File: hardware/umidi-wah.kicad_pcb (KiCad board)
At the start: 2 copper layers, 100.7 x 113.4 mm, 83 parts, among them J1 Conn_01x02, J11 Pots Main, J12 Pots Front, J4 Conn_01x02, J5 Input, J6 Output, J7 Conn_02x05_Odd_Even, J8 Conn_02x05_Odd_Even, K1 G6K-2P-Y-DC5, Q1 KSC1815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

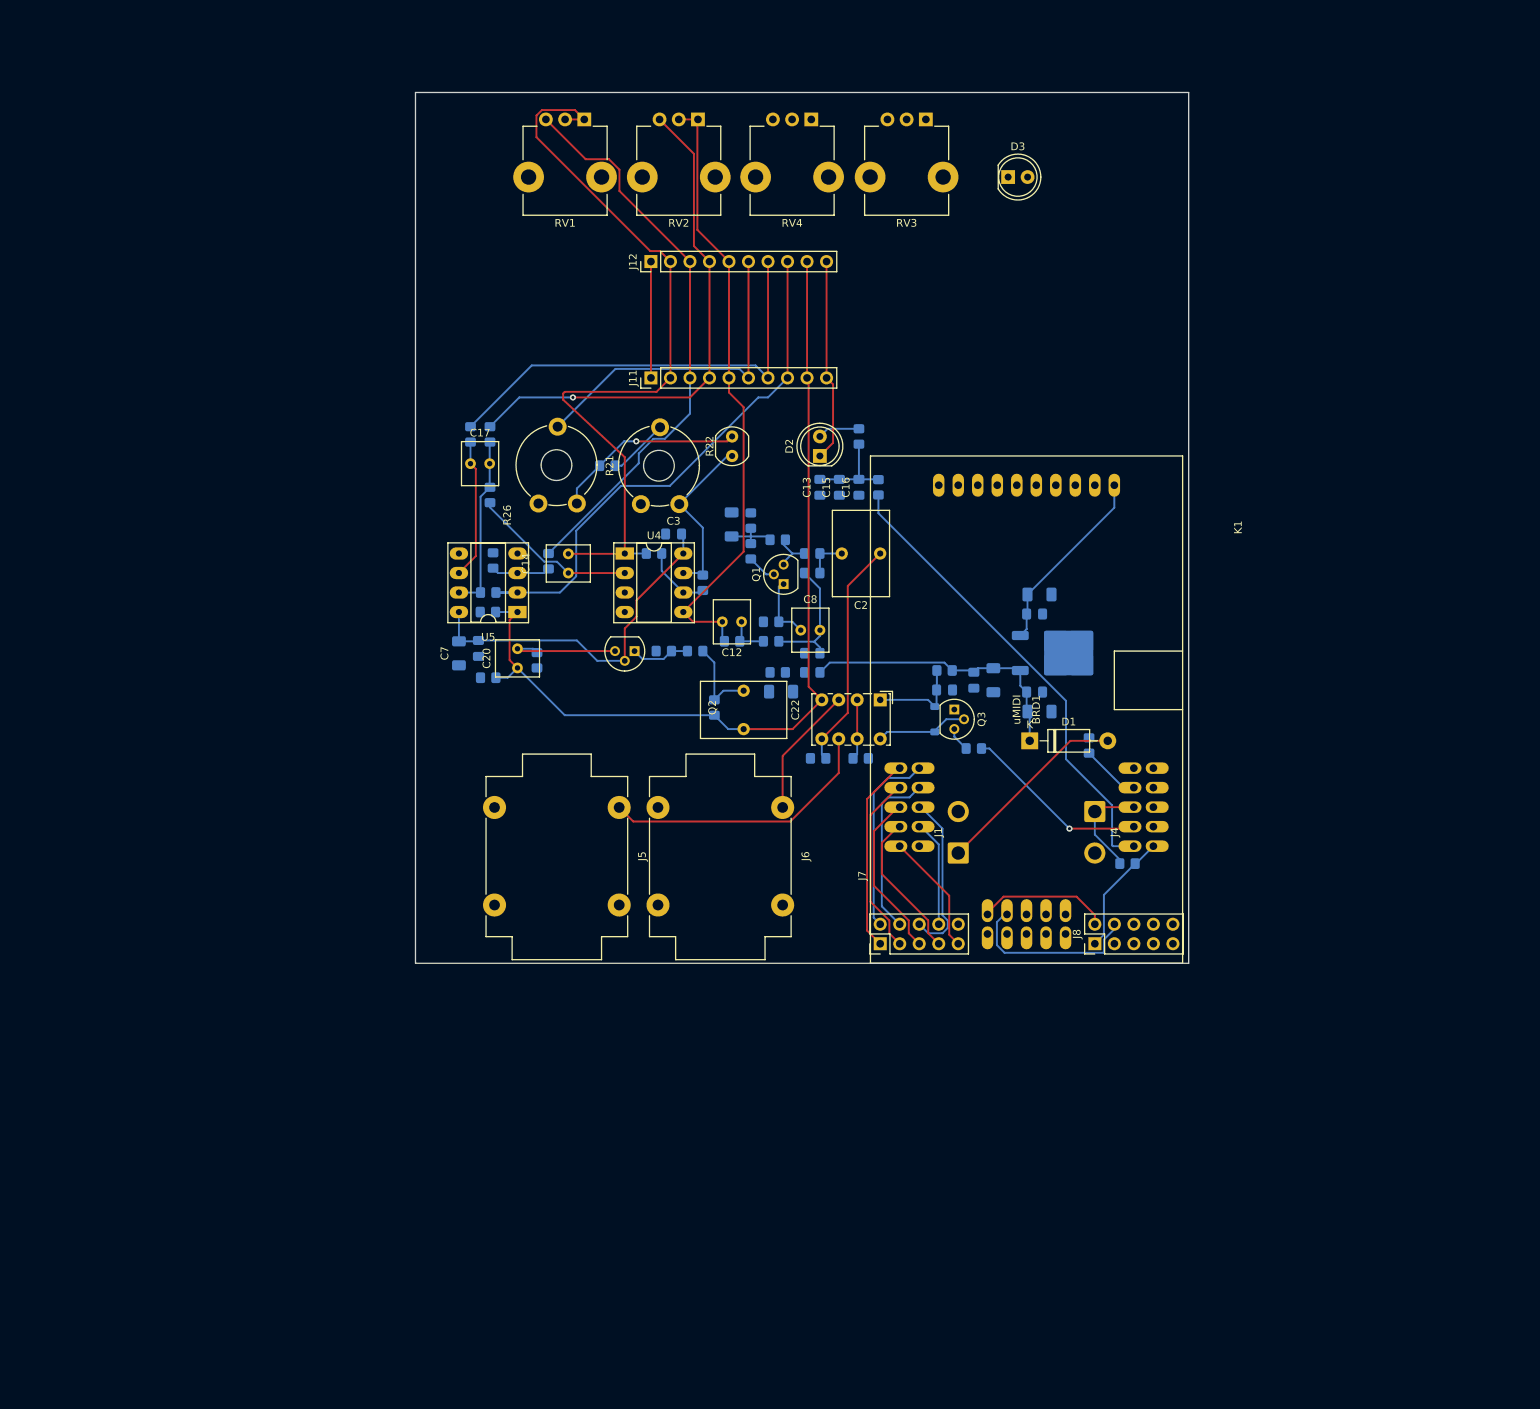
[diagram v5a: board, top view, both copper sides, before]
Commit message: Route pretty much everything
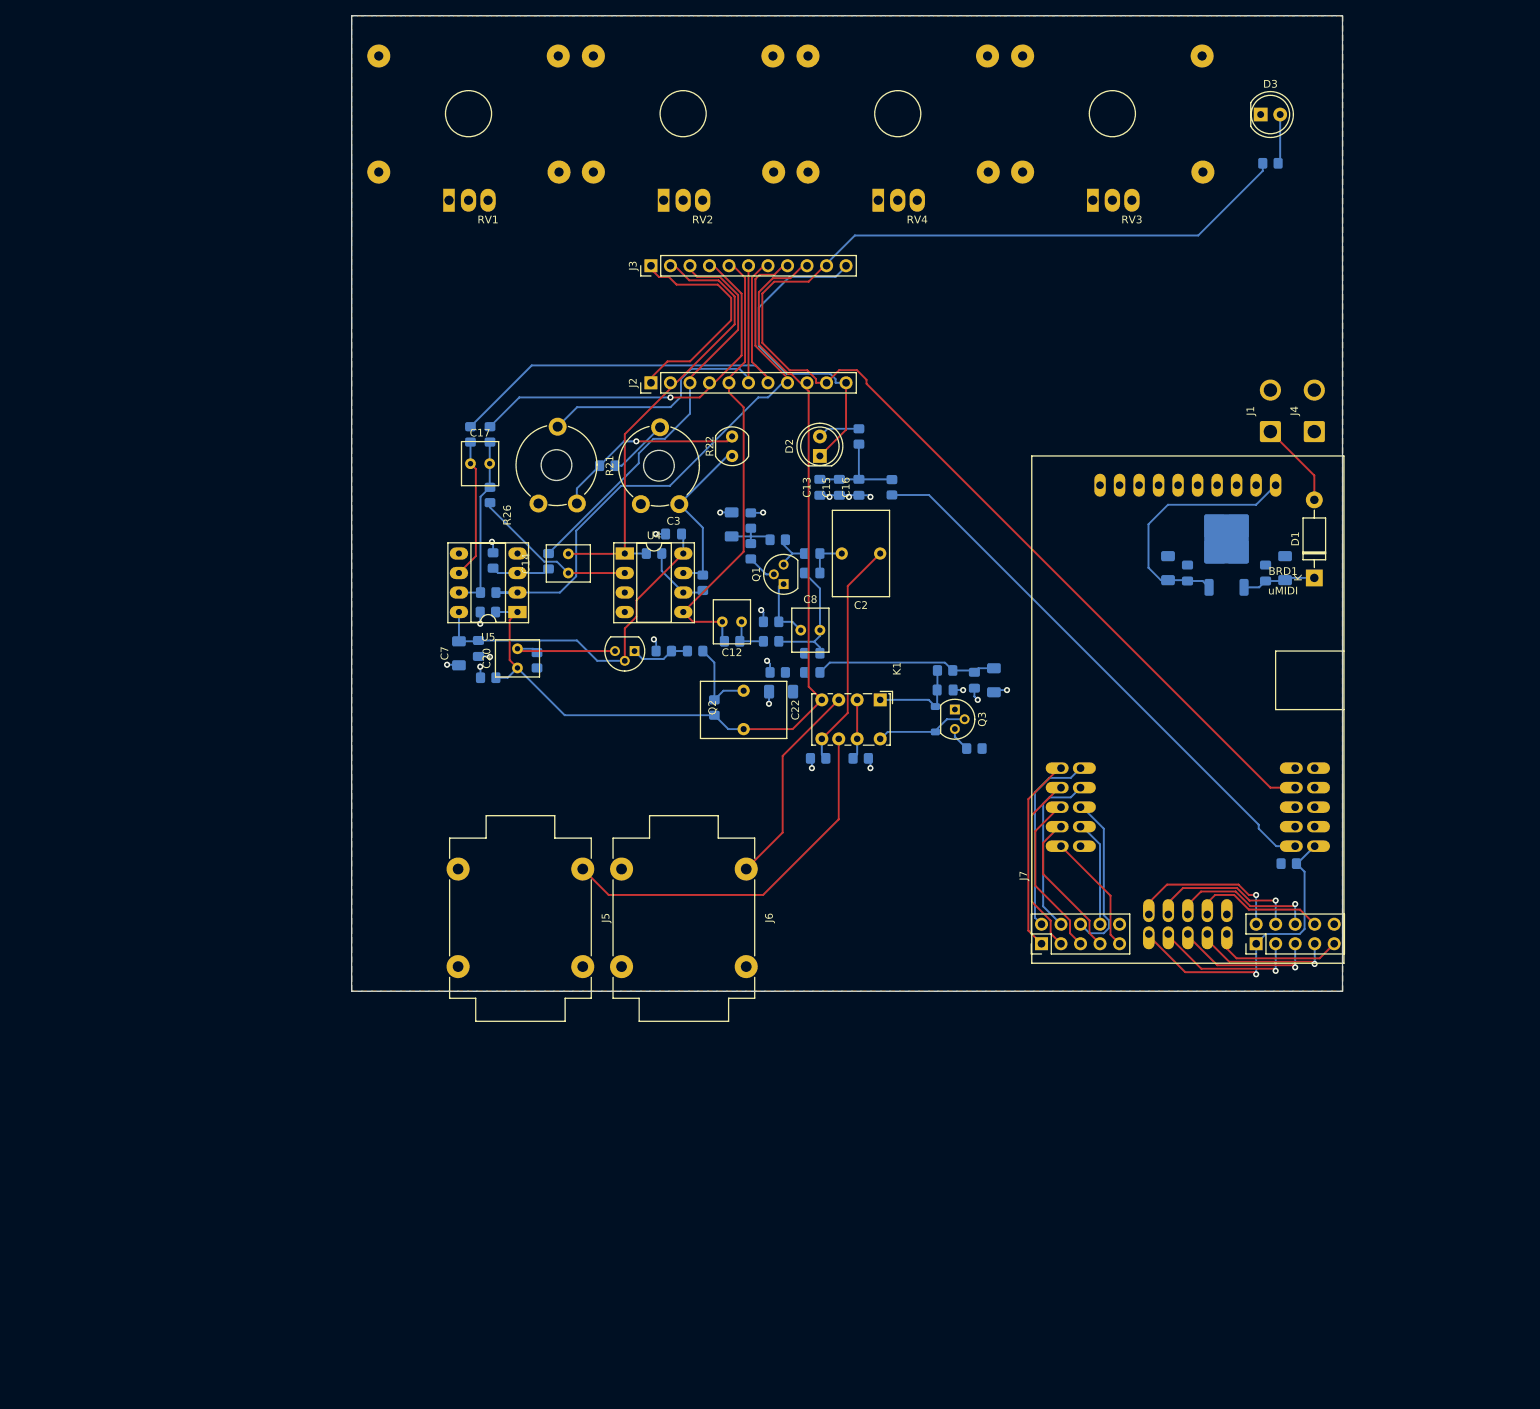
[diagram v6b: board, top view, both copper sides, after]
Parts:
- removed J11: Pots Main, Connector_PinHeader_2.54mm:PinHeader_1x10_P2.54mm_Vertical
- removed J12: Pots Front, Connector_PinHeader_2.54mm:PinHeader_1x10_P2.54mm_Vertical
- added J2: Pots Main, Connector_PinHeader_2.54mm:PinHeader_1x11_P2.54mm_Vertical, F.Cu at (101.0, 57.8)
- added J3: Pots Front, Connector_PinHeader_2.54mm:PinHeader_1x11_P2.54mm_Vertical, F.Cu at (101.0, 42.5)
- J1: value Conn_01x02 -> Power
- J4: value Conn_01x02 -> Switch
- RV1, RV2, RV3, RV4: footprint Potentiometer_THT:Potentiometer_TT_P0915N -> uMidi-wah:Bourns PC Axial Rear Mounting Bracket
- moved R24 79.4 mm to (181.6, 29.2), turned to 180 degrees
- moved J1 68.3 mm to (181.6, 64.1)
- moved J4 57.1 mm to (187.3, 64.1), turned to 90 degrees
- moved D1 42.7 mm to (187.3, 83.2), turned to 90 degrees
- moved C4 37.0 mm to (183.5, 81.9), turned to 90 degrees
- moved D3 33.9 mm to (180.3, 22.9)
- moved C5 33.8 mm to (181.0, 82.5), turned to 90 degrees
- moved RV3 26.5 mm to (161.0, 34.0), turned to 0 degrees
- moved U3 25.7 mm to (175.9, 79.4), turned to 90 degrees
- moved BRD1 21.0 mm to (170.9, 100.3)
- moved J7 21.0 mm to (151.8, 130.8)
- moved J8 21.0 mm to (179.8, 130.8)
- moved R25 21.0 mm to (184.0, 120.4)
- moved C9 20.6 mm to (170.8, 82.5), turned to 90 degrees
- moved RV1 18.4 mm to (77.2, 34.0), turned to 0 degrees
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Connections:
- net /status_led renamed /Filter/status_led
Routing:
- net /Filter/status_led: track 7.69 -> 175.8 mm
- net GND: track 41.5 -> 105.8 mm, vias 0 -> 20
- net /Filter/rv1_1: track 101.0 -> 59.8 mm
- net /bypass_n: track 24.9 -> 0.60 mm, vias 1 -> 0
- net /umidi_3v3: track 41.4 -> 65.1 mm, vias 0 -> 1
- net /Filter/rv1_2: track 75.0 -> 52.8 mm
- net /Filter/rv2_1: track 80.7 -> 59.7 mm
- net Net-(BRD1C-PB1): track 0.00 -> 19.6 mm, vias 0 -> 1
- net Net-(BRD1C-PC0(SDA)): track 0.00 -> 19.5 mm, vias 0 -> 1
- net Net-(BRD1C-PB3(DACB::DAC1)): track 0.00 -> 19.0 mm, vias 0 -> 1
- net Net-(BRD1C-PC1(SCL)): track 0.00 -> 18.7 mm, vias 0 -> 1
- net Net-(BRD1C-PC2(C0::RXD0)): track 0.00 -> 17.5 mm
- net Net-(BRD1C-PC3(C0::TXD0)): track 0.00 -> 17.2 mm
- net /Filter/rv2_2: track 67.5 -> 50.6 mm
- net Net-(D1-A): track 25.5 -> 11.3 mm
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- added copper zone on B.Cu, net GND
- added copper zone on F.Cu, net GND
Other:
- board size 100.7 x 113.4 mm -> 129 x 127 mm

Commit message: Replace bourns potentiometers in schematic and board
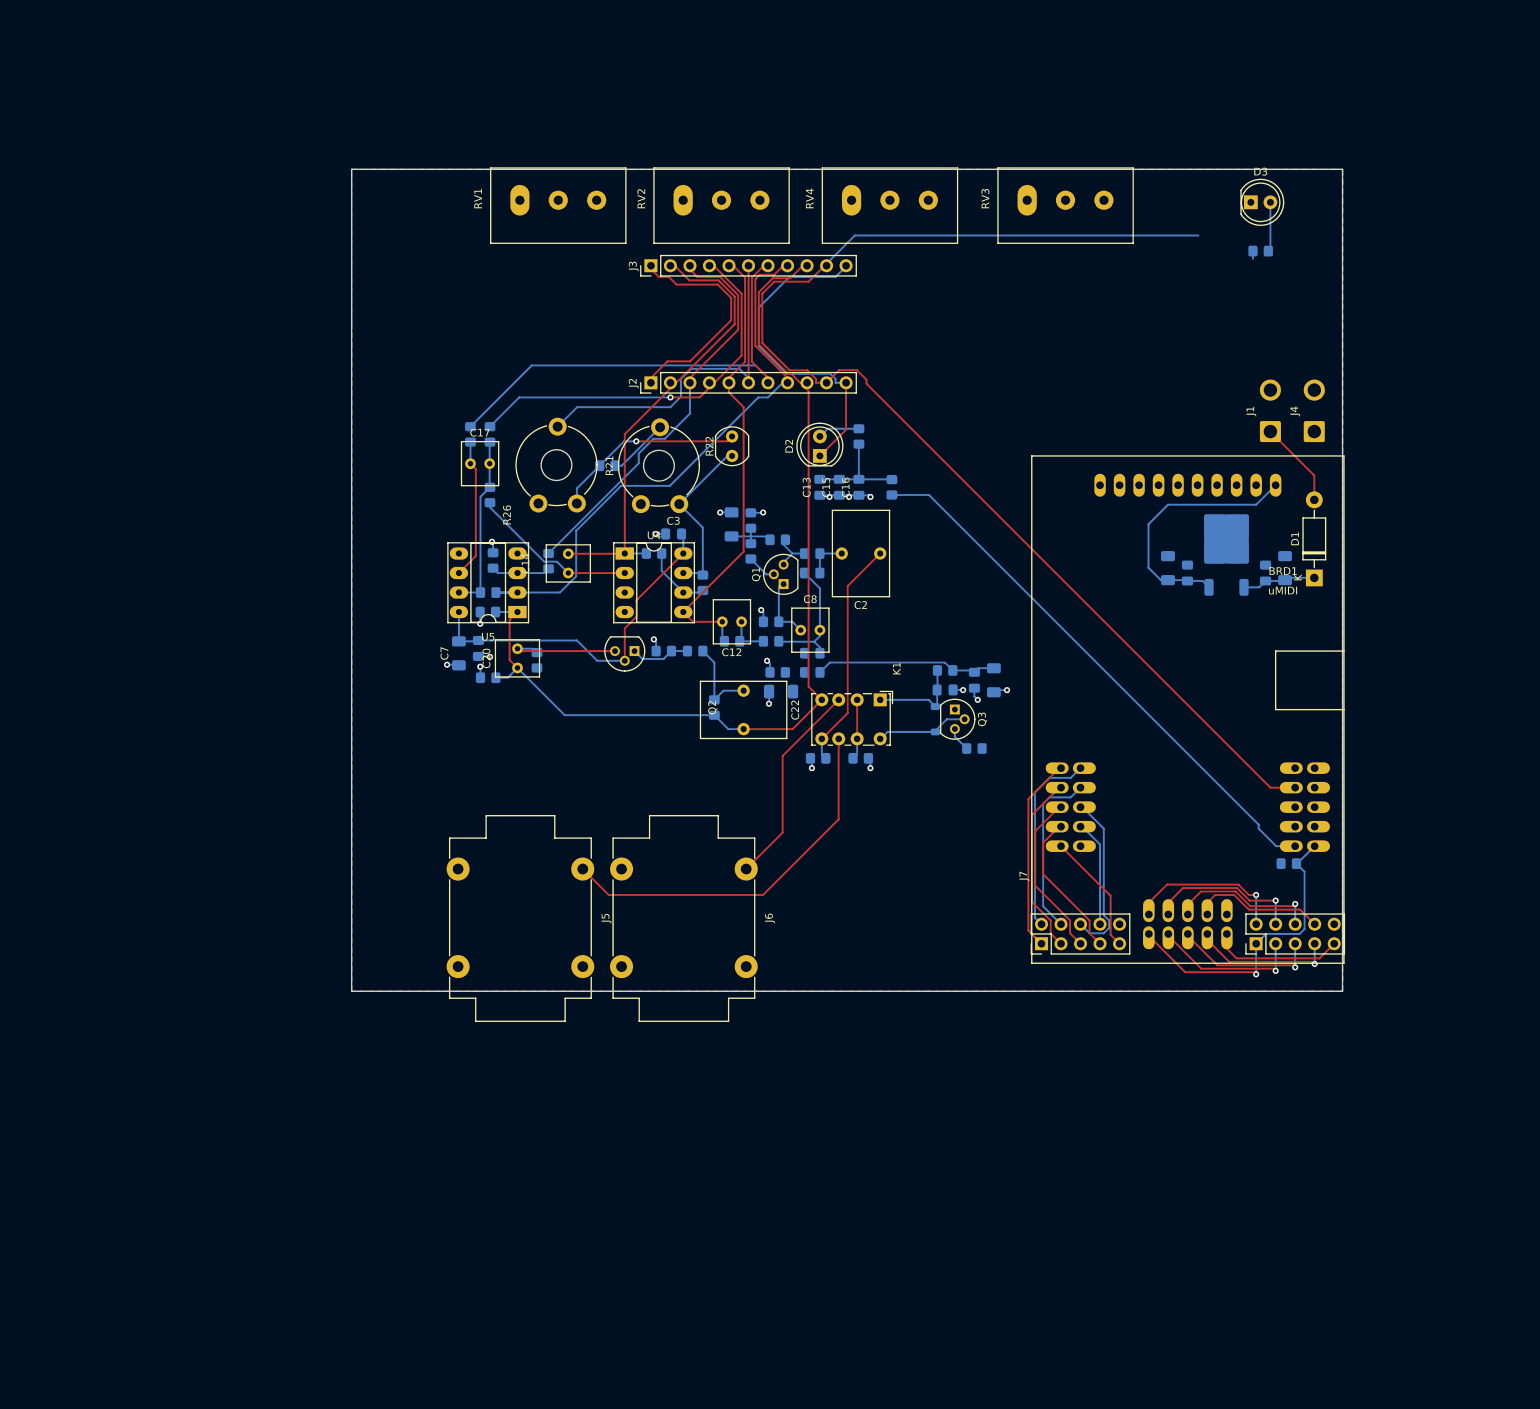
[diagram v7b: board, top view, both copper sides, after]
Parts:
- RV1: value 100k -> 100k, Anti-Log; footprint uMidi-wah:Bourns PC Axial Rear Mounting Bracket -> uMidi-wah:Potentiometer_Alpha_RV16AF-20-15k-Single_Horizontal
- RV2: value 250k -> 250k, Log; footprint uMidi-wah:Bourns PC Axial Rear Mounting Bracket -> uMidi-wah:Potentiometer_Alpha_RV16AF-20-15k-Single_Horizontal
- RV3: value 10k -> 10k, Lin; footprint uMidi-wah:Bourns PC Axial Rear Mounting Bracket -> uMidi-wah:Potentiometer_Alpha_RV16AF-20-15k-Single_Horizontal
- RV4: value 2.5k -> 50k, Anti-Log; footprint uMidi-wah:Bourns PC Axial Rear Mounting Bracket -> uMidi-wah:Potentiometer_Alpha_RV16AF-20-15k-Single_Horizontal
- moved D3 11.5 mm to (179.1, 34.3)
- moved R24 11.5 mm to (180.3, 40.6)
- moved RV3 11.1 mm to (149.9, 34.0), turned to 90 degrees
- moved RV1 6.69 mm to (83.9, 34.0), turned to 90 degrees
- moved RV4 6.02 mm to (127.1, 34.0), turned to 90 degrees
- turned RV2 to 90 degrees
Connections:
- RV2 pad 2: /Filter/rv2_1 -> /Filter/rv2_2
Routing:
- net /Filter/status_led: track 175.8 -> 163.9 mm
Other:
- board size 129 x 127 mm -> 129 x 107 mm

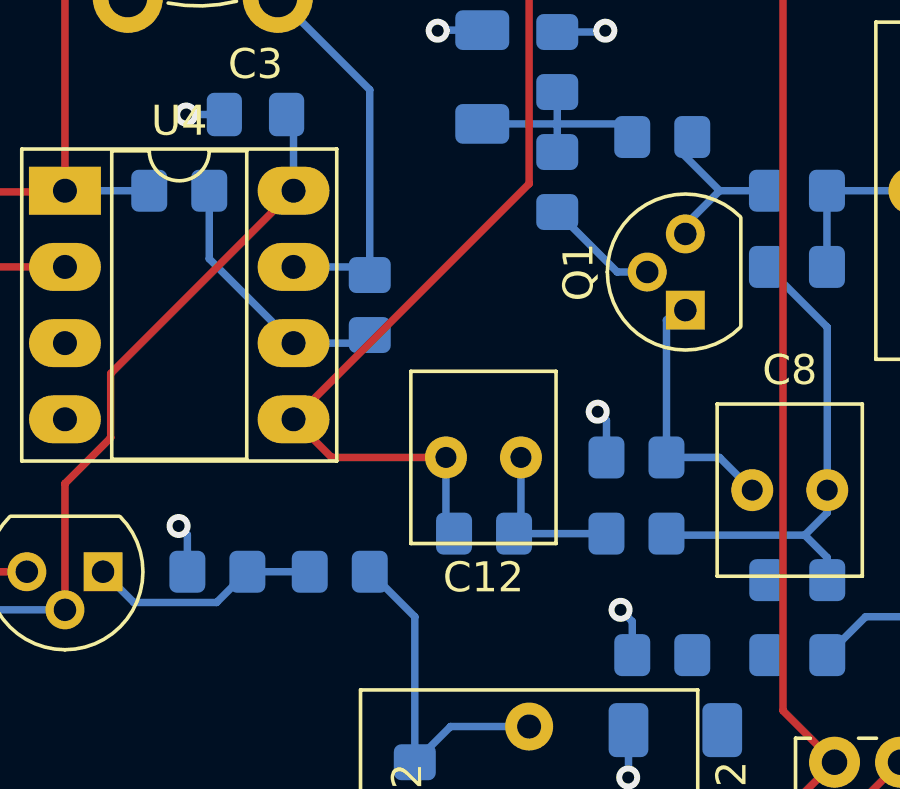
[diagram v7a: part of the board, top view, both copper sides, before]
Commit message: Add supplier link; Change footprint of 18n film cap
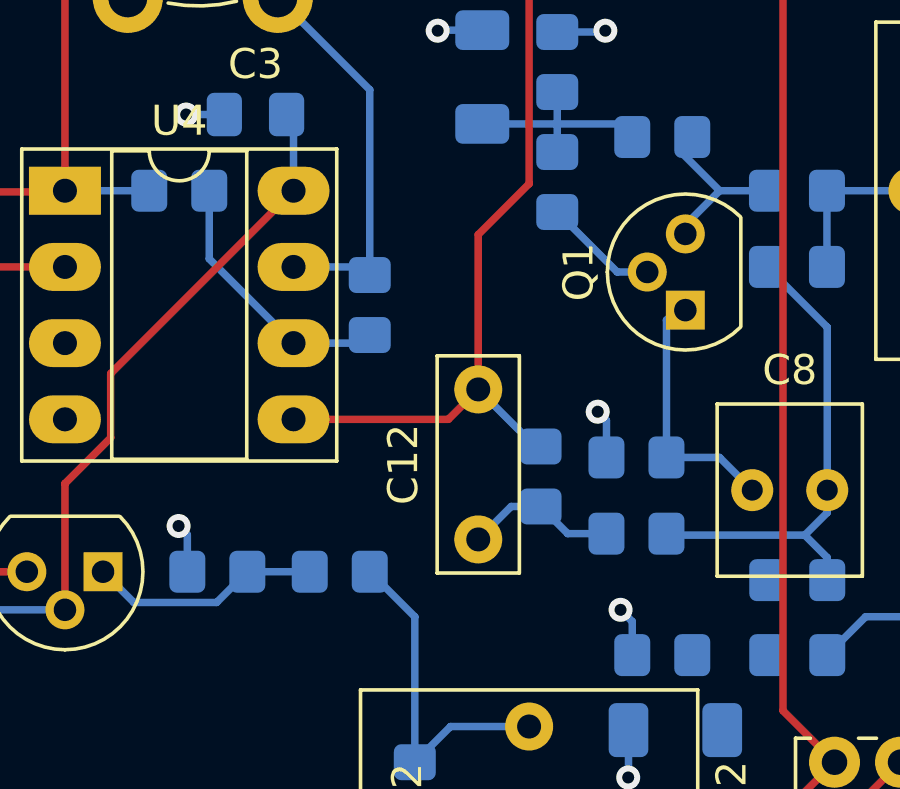
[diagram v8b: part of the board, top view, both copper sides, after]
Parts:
- C12: footprint Capacitor_THT:C_Rect_L4.6mm_W5.5mm_P2.50mm_MKS02_FKP02 -> Capacitor_THT:C_Rect_L7.0mm_W2.5mm_P5.00mm
- moved C12 3.08 mm to (111.3, 91.6), turned to 90 degrees
- moved R11 2.68 mm to (113.4, 89.5), turned to 90 degrees
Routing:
- net /Filter/rv2_1: track 59.7 -> 57.3 mm
- net Net-(C12-Pad1): track 5.72 -> 5.10 mm
